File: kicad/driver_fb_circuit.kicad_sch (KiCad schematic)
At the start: 42 parts, among them Q1 IRFZ44N, Q2 IRFZ44N, Q3 IRFZ44N, Q4 IRFZ44N, Q5 IRFZ44N, Q6 IRFZ44N, U1 IR2104, U2 IR2104, U3 IR2104, U4 INA180A2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

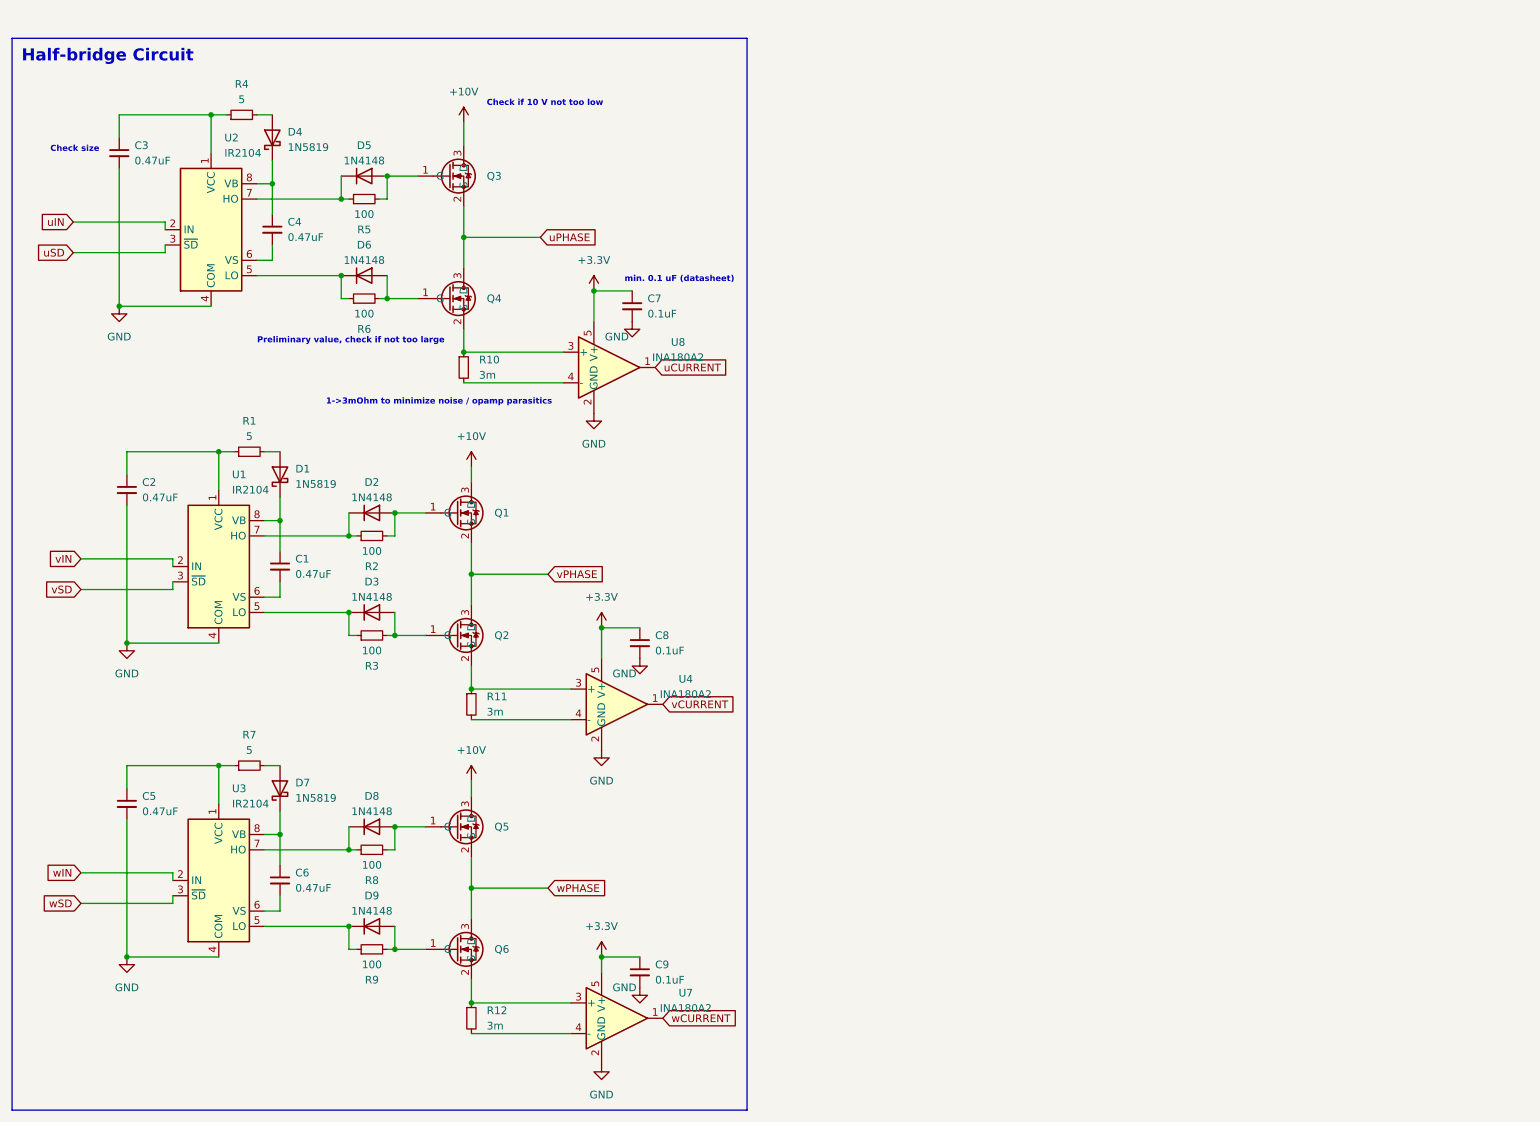
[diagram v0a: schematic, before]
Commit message: [kicad] Added resistive bridge + virtual star for back-EMF meausrement, [cubemx] Added cubemx configuration file |TODO| Check ADC-DMA, ADC-CMP and interrupt with ADC functions, ADC-DMA
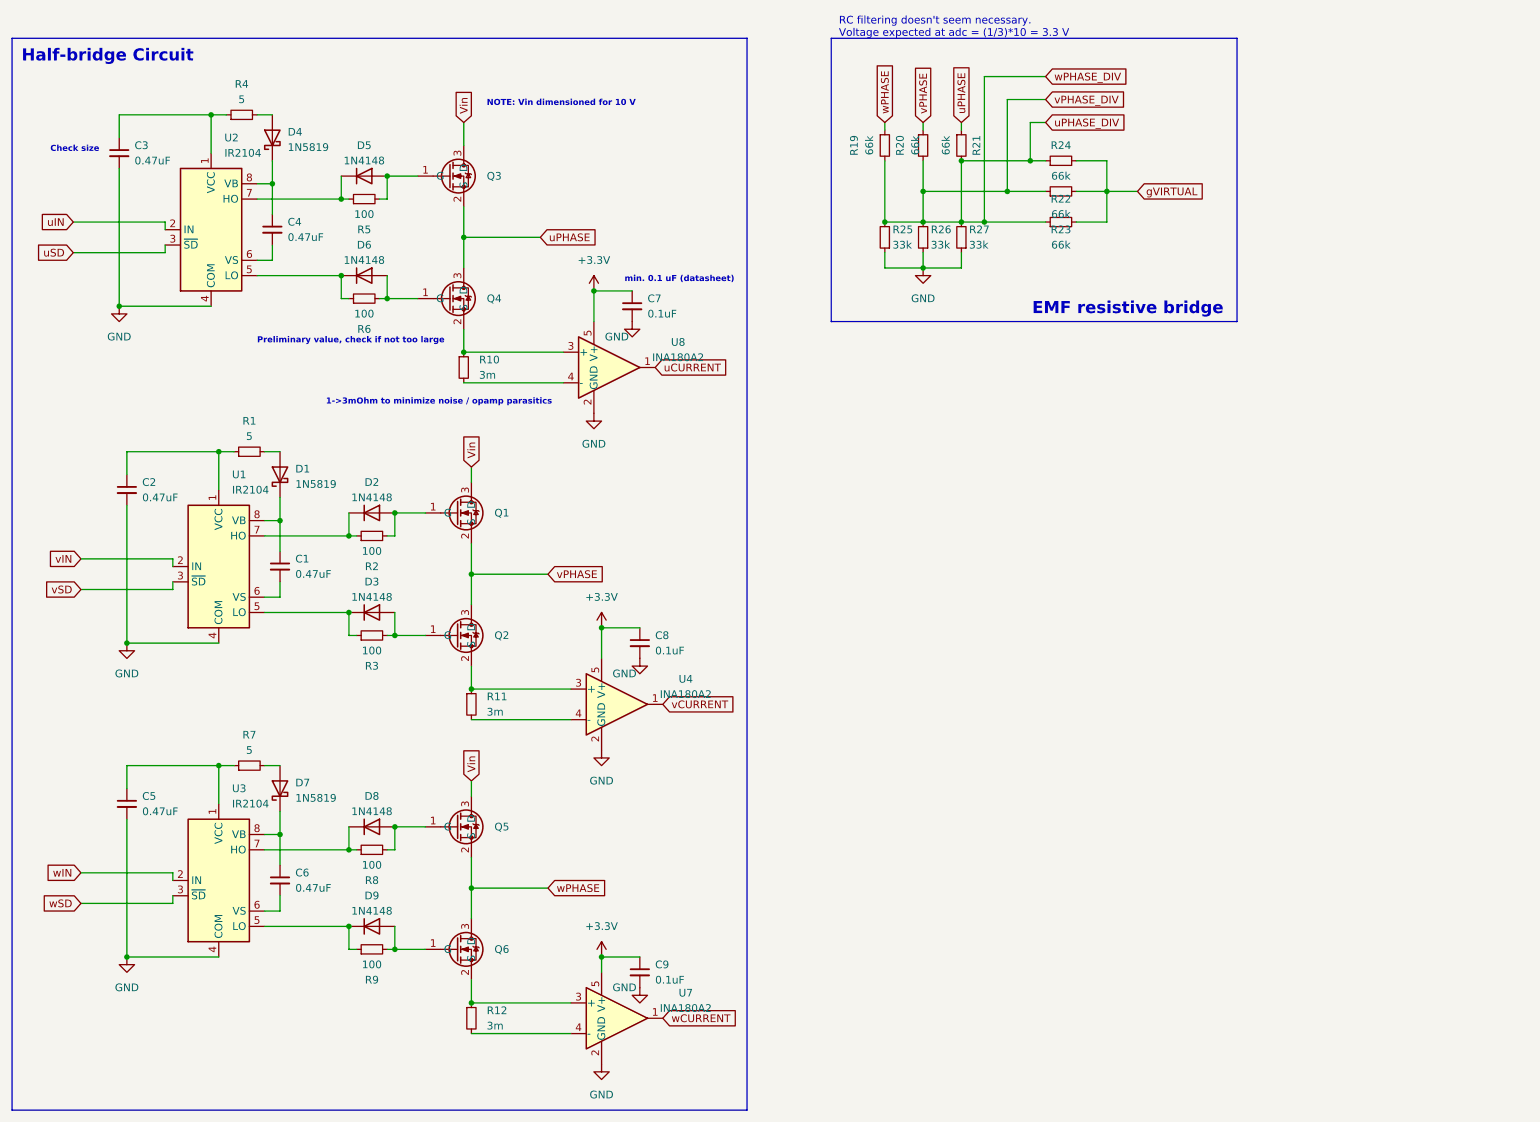
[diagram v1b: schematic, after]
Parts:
- added R19, R20, R21, R22, R23, R24: 66k, symbol Device:R_Small
- added R25, R26, R27: 33k, symbol Device:R_Small
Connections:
- net GND: now also R25.1, R26.1, R27.1
- net uPHASE: now also R21.1
- net vPHASE: now also R20.1
- net wPHASE: now also R19.1
- net +10V renamed Vin
- new net gVIRTUAL: R22.2, R23.2, R24.2
- new net uPHASE_DIV: R19.2, R20.2, R21.2, R22.1, R23.1, R24.1, R25.2, R26.2, R27.2
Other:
- note added: "NOTE: Vin dimensioned for 10 V"
- note added: "RC filtering doesn't seem necessary. Voltage expected at adc = (1/3)*10 = 3.3 V"
- note removed: "Check if 10 V not too low"

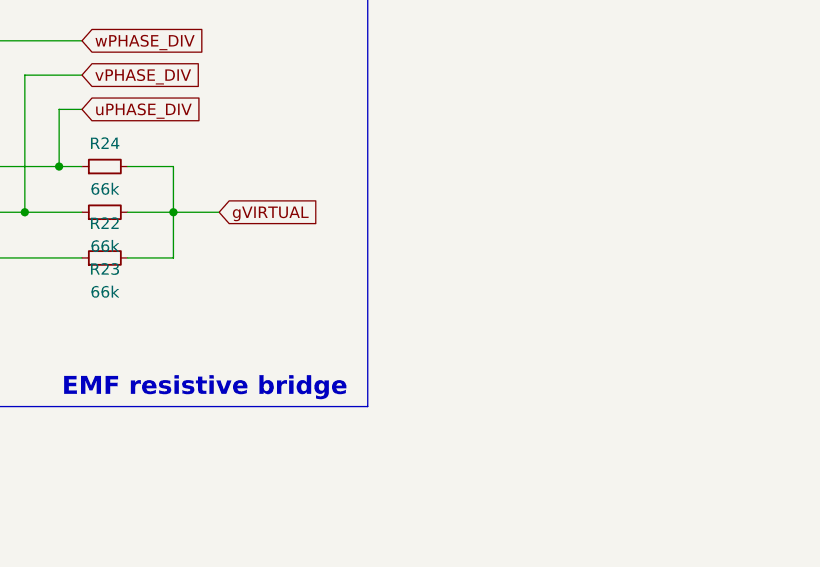
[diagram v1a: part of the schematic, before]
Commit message: [kicad] Added ADC_in, PWM_out labels as well as thermistor + battery management voltage divider | TODO: search for thermistor + CAN-circuit
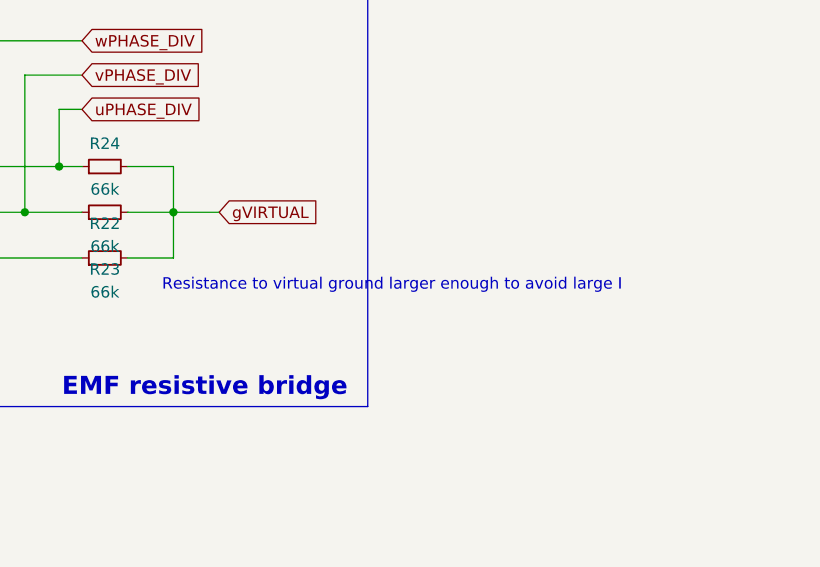
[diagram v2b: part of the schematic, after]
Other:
- note added: "Resistance to virtual ground larger enough to avoid large I"
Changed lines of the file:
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@@
     (effects (font (size 1 1) bold) (justify left bottom))
+  )
+  (text "Resistance to virtual ground larger enough to avoid large I"
+    (at 200.66 52.07 0)
+    (effects (font (size 1.27 1.27)) (justify left bottom))
   )
   (text "NOTE: Vin dimensioned for 10 V\n" (at 99.06 29.21 0)

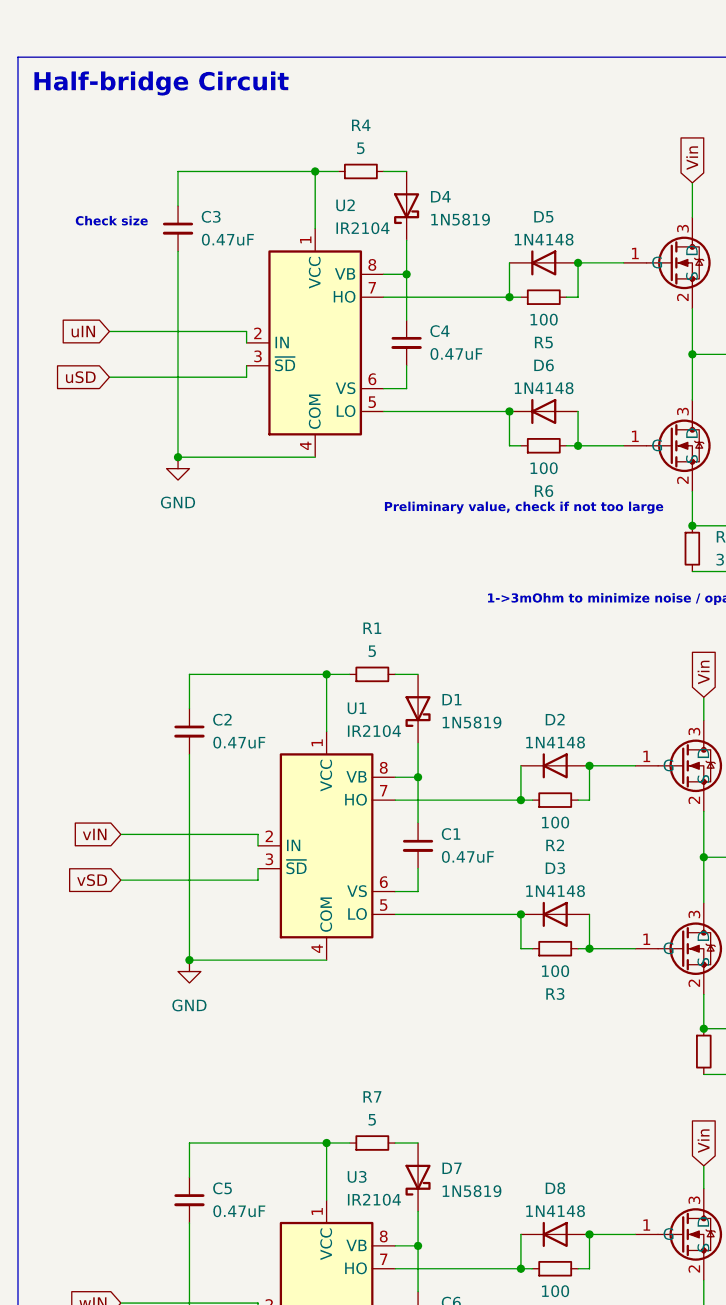
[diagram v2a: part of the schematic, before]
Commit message: [kicad] Added i2c connection
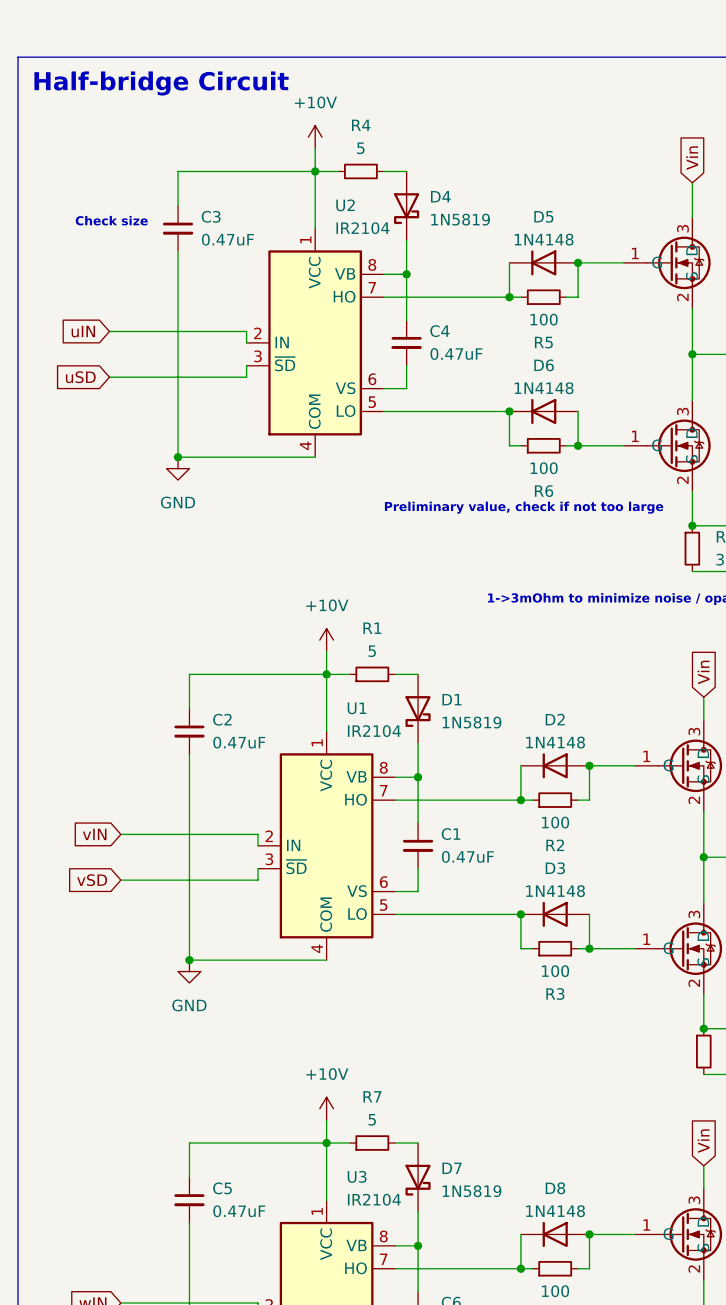
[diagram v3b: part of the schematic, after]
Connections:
- net +10V: now reaches C5.1, R7.1, U3.1 (VCC)
- net +10V: now also C2.1, C3.1, R1.1, R4.1, U1.1 (VCC), U2.1 (VCC)
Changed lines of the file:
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@@
+    (stroke (width 0) (type default))
+  )
+  (wire (pts (xy 53.34 27.94) (xy 53.34 30.48))
     (stroke (width 0) (type default))
   )
@@
     (stroke (width 0) (type default))
   )
+  (wire (pts (xy 54.61 83.82) (xy 54.61 86.36))
+    (stroke (width 0) (type default))
+  )
   (wire (pts (xy 39.37 142.24) (xy 39.37 138.43))
     (stroke (width 0) (type default))
@@
   )
   (wire (pts (xy 82.55 60.96) (xy 82.55 57.15))
+    (stroke (width 0) (type default))
+  )
+  (wire (pts (xy 54.61 135.89) (xy 54.61 138.43))
     (stroke (width 0) (type default))
   )
@@
     )
   )
+  (symbol (lib_id "power:+10V") (at 54.61 83.82 0) (unit 1)
+    (in_bom yes) (on_board yes) (dnp no) (fields_autoplaced)
+    (property "Reference" "#PWR046" (at 54.61 87.63 0)
+      (effects (font (size 1.27 1.27)) hide)
+    )
+    (property "Value" "+10V" (at 54.61 78.74 0)
+      (effects (font (size 1.27 1.27)))
+    )
+    (property "Footprint" "" (at 54.61 83.82 0)
+      (effects (font (size 1.27 1.27)) hide)
+    )
+    (property "Datasheet" "" (at 54.61 83.82 0)
+      (effects (font (size 1.27 1.27)) hide)
+    )
+    (pin "1")
+    (instances
+      (project "bldc_project"
+        (path "/91e2f46a-700b-4d7a-a06a-22469f63223f/7f7e17e0-7d73-4fbb-9112-49949fae378a"
+          (reference "#PWR046") (unit 1)
+        )
+      )
+    )
+  )
   (symbol (lib_id "power:+3.3V") (at 118.11 115.57 0) (unit 1)
     (in_bom yes) (on_board yes) (dnp no) (fields_autoplaced)
@@
     )
   )
+  (symbol (lib_id "power:+10V") (at 53.34 27.94 0) (unit 1)
+    (in_bom yes) (on_board yes) (dnp no) (fields_autoplaced)
+    (property "Reference" "#PWR042" (at 53.34 31.75 0)
+      (effects (font (size 1.27 1.27)) hide)
+    )
+    (property "Value" "+10V" (at 53.34 22.86 0)
+      (effects (font (size 1.27 1.27)))
+    )
+    (property "Footprint" "" (at 53.34 27.94 0)
+      (effects (font (size 1.27 1.27)) hide)
+    )
+    (property "Datasheet" "" (at 53.34 27.94 0)
+      (effects (font (size 1.27 1.27)) hide)
+    )
+    (pin "1")
+    (instances
+      (project "bldc_project"
+        (path "/91e2f46a-700b-4d7a-a06a-22469f63223f/7f7e17e0-7d73-4fbb-9112-49949fae378a"
+          (reference "#PWR042") (unit 1)
+        )
+      )
+    )
+  )
   (symbol (lib_id "Driver_FET:IR2104") (at 54.61 157.48 0) (unit 1)
     (in_bom yes) (on_board yes) (dnp no) (fields_autoplaced)
@@
         )
       )
+    )
+  )
+  (symbol (lib_id "power:+10V") (at 54.61 135.89 0) (unit 1)
+    (in_bom yes) (on_board yes) (dnp no) (fields_autoplaced)
+    (property "Reference" "#PWR047" (at 54.61 139.7 0)
+      (effects (font (size 1.27 1.27)) hide)
+    )
+    (property "Value" "+10V" (at 54.61 130.81 0)
+      (effects (font (size 1.27 1.27)))
+    )
+    (property "Footprint" "" (at 54.61 135.89 0)
+      (effects (font (size 1.27 1.27)) hide)
+    )
+    (property "Datasheet" "" (at 54.61 135.89 0)
+      (effects (font (size 1.27 1.27)) hide)
+    )
+    (pin "1")
+    (instances
+      (project "bldc_project"
+        (path "/91e2f46a-700b-4d7a-a06a-22469f63223f/7f7e17e0-7d73-4fbb-9112-49949fae378a"
+          (reference "#PWR047") (unit 1)
+        )
+      )

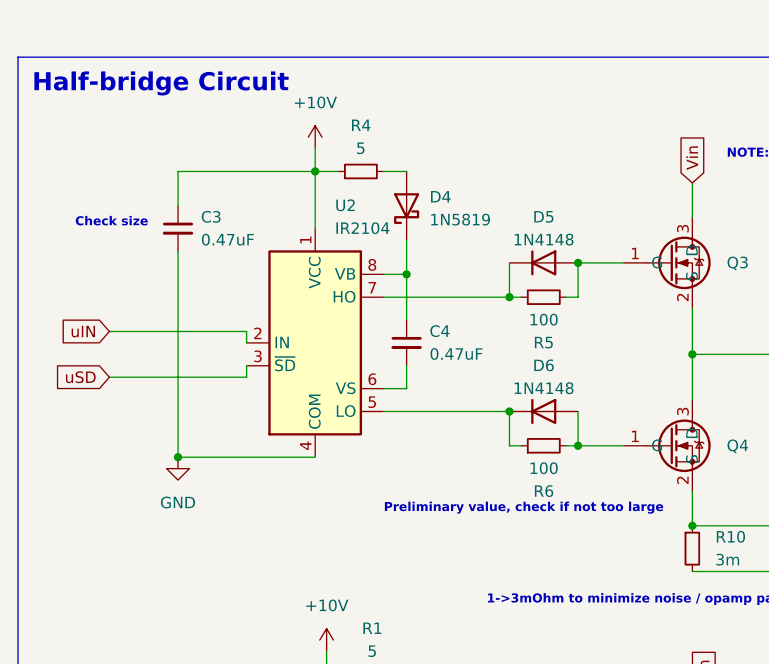
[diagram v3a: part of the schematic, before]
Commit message: [ltspice] added MC34063 simulation model
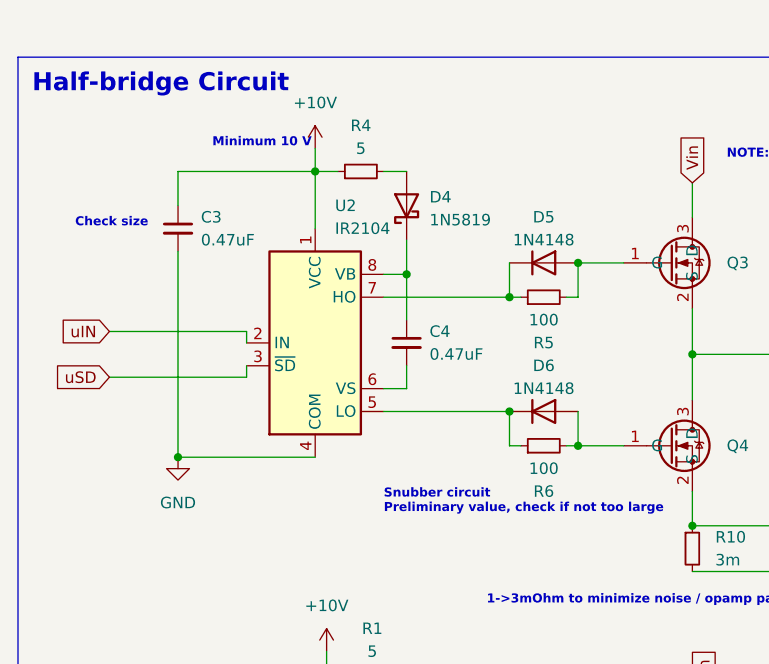
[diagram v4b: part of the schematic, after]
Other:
- note added: "Minimum 10 V"
- note added: "Snubber circuit Preliminary value, check if not too large"
- note removed: "Preliminary value, check if not too large"
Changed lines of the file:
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@@
     (effects (font (size 1 1) bold) (justify left bottom))
   )
-  (text "Preliminary value, check if not too large" (at 60.96 68.58 0)
+  (text "Minimum 10 V" (at 41.91 27.94 0)
     (effects (font (size 1 1) bold) (justify left bottom))
   )
+  (text "Snubber circuit\nPreliminary value, check if not too large"
+    (at 60.96 68.58 0)
+    (effects (font (size 1 1) bold) (justify left bottom))
+  )
